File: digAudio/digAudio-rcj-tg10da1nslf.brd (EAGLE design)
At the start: 18.8 x 19.7 mm, 12 parts, among them IC1 DIT4096-H

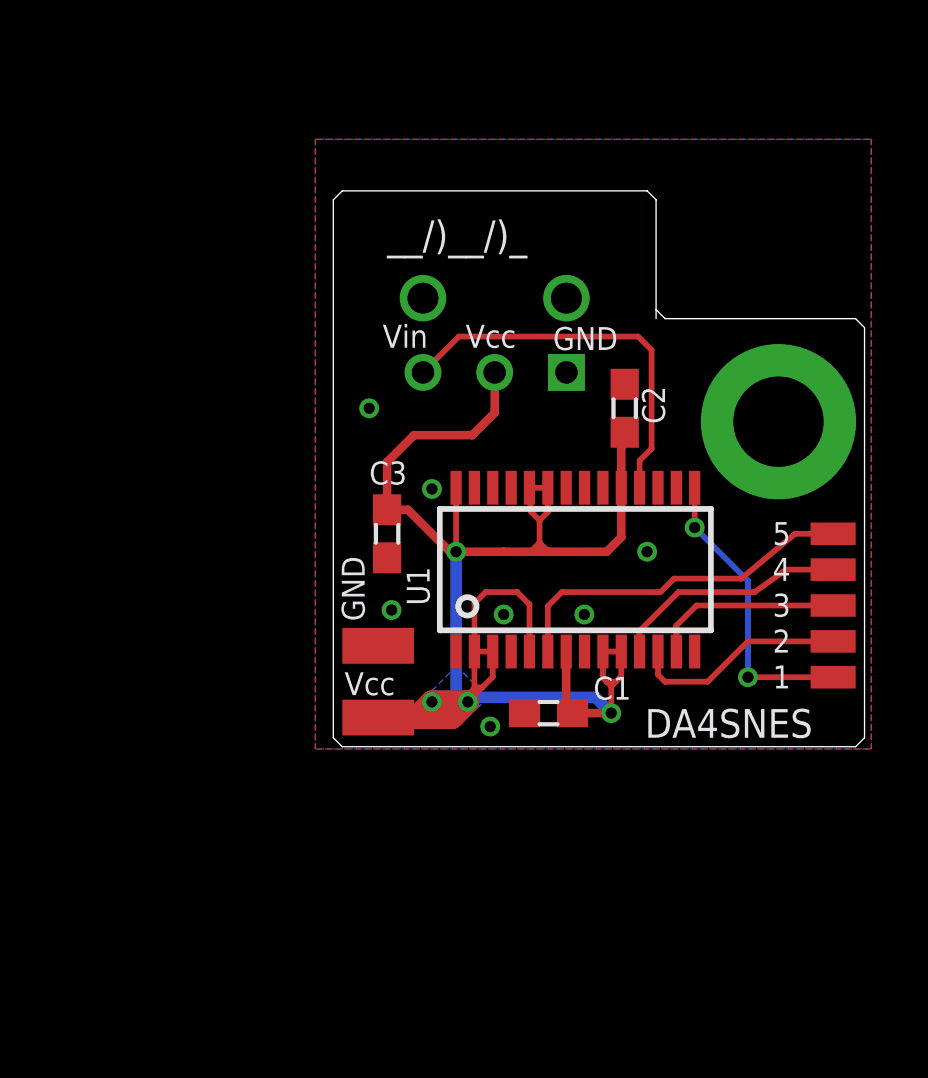
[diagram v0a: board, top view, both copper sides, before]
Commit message: update digital audio mod incl a new no-cut design with coax
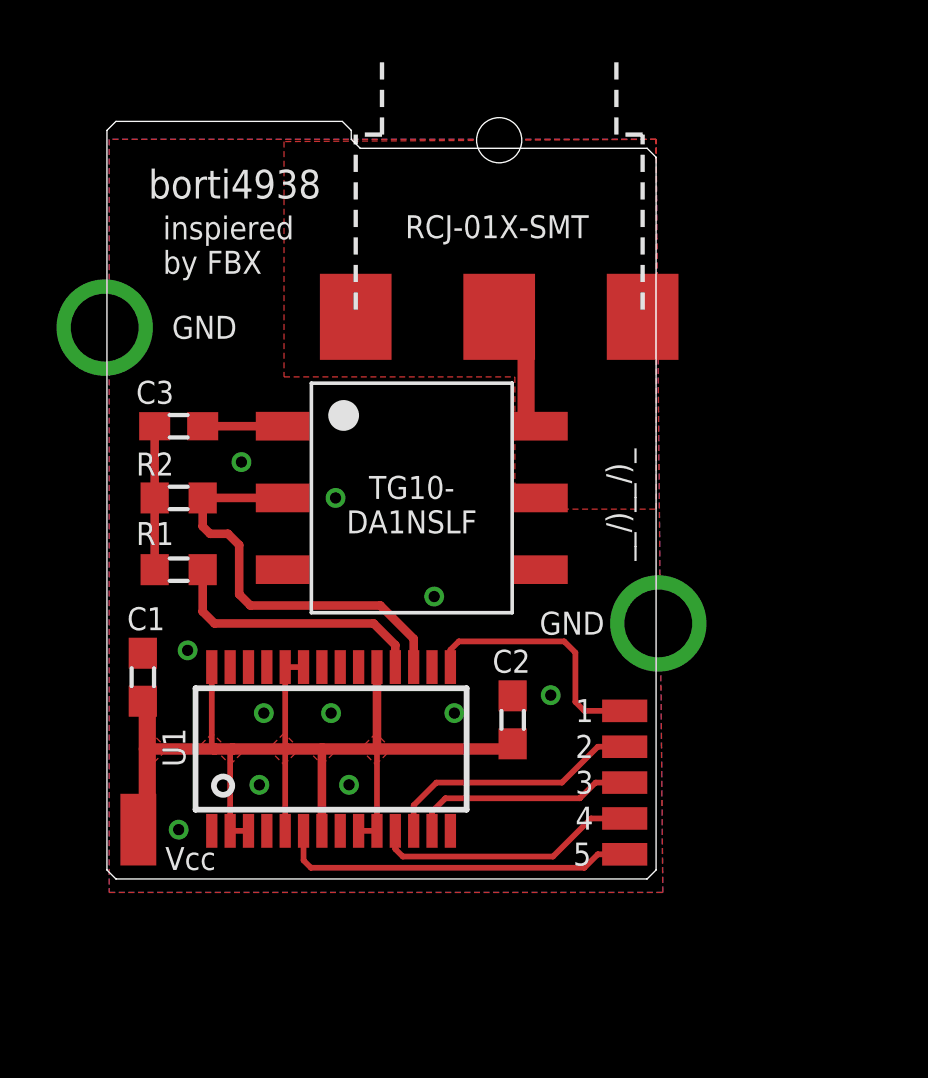
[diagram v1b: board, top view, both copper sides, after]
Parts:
- removed GND: (no value), wirepad:SMD1,27-2,54
- added R1: 360, rcl:R0603
- added R2: 91, rcl:R0603
- added U$2: TG10-DA1NSLF, cs8406:TG10-DA1NSFL
- C3: value 0.1uF -> 10nF
- U$1: value PLT133/T10W -> RCJ-013-SMT-TR; device cs8406:PLT133/T10W -> digAudio_SNES:RCJ_01X_SMT_MODIFIED
- moved C1 14.4 mm to (-6.11, 2.54), turned to 90 degrees
- moved 5 13.5 mm to (11.0, -3.73)
- moved C2 11.7 mm to (6.99, 1.03)
- moved 4 11.5 mm to (11.0, -2.46)
- moved IC1 10.7 mm to (0.56, 0.00)
- moved 3 9.69 mm to (11.0, -1.19)
- moved VCC 9.37 mm to (-6.27, -2.86), turned to 180 degrees
- moved C3 8.31 mm to (-4.84, 11.4), turned to 0 degrees
- moved 2 8.27 mm to (11.0, 0.08)
- moved 1 7.48 mm to (11.0, 1.35)
- moved U$1 2.23 mm to (6.51, 15.6), flipped to the top, turned to 270 degrees
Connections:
- new net N$10: U$1.1A, U$1.1B, U$2.5
- new net N$11: C3.2, U$2.1
- new net N$7: IC1.17, R2.1, U$2.2
- new net N$8: C3.1, R1.2, R2.2
- new net N$9: U$1.2, U$2.6
- net GND: now also U$2.3; no longer C3.2, GND.1, U$1.P$1
- net N$1: now also R1.1; no longer U$1.P$3
- net VCC: no longer C3.1, U$1.P$2
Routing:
- net VCC: track 66.8 -> 40.3 mm, vias 4 -> 0
- net N$7: track 0.00 -> 15.0 mm
- net N$9: track 0.00 -> 5.35 mm
- net N$8: track 0.00 -> 5.08 mm
- net N$1: track 13.9 -> 9.58 mm
- net N$11: track 0.00 -> 2.83 mm
- net N$2: track 10.5 -> 8.95 mm, vias 2 -> 0
- net N$3: track 7.72 -> 9.24 mm
- net N$5: track 6.77 -> 7.93 mm
- net N$4: track 8.41 -> 9.44 mm
- added copper zone on layer 1, net N$10
- added copper zone on layer 1, net VCC
- removed copper zone on layer 16, net VCC
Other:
- board size 18.8 x 19.7 mm -> 19.4 x 26.8 mm
- board text added: "Digital Audio for SNES RCA-output version"
- board text added: "R1"
- board text added: "R2"
- board text added: "RCJ-01X-SMT"
- board text added: "TG10- DA1NSLF"
- board text added: "borti4938"
- board text added: "inspiered by FBX"
- board text removed: "DA4SNES"
- board text removed: "Vin"

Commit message: PCB Update
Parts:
- added GND: (no value), wirepad:1,6/0,9
- added J1: (no value), jumper:SJ_2
- C3: value 10nF -> 10nF/0.1uF
- R1: value 360 -> 347.5/57
- R2: value 91 -> 90.9/open
- VCC: device wirepad:SMD1,27-2,54 -> wirepad:1,6/0,9
- moved VCC 12.7 mm to (5.00, -8.81), turned to 0 degrees
- moved C3 2.29 mm to (-3.57, 13.3)
- moved R2 1.02 mm to (-5.48, 9.68), turned to 270 degrees
- moved R1 0.75 mm to (-5.48, 6.75), turned to 90 degrees
- moved U$2 0.63 mm to (4.05, 8.89)
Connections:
- new net N$12: J1.2, R2.1, U$2.2
- net GND: now also GND.1, J1.1
- net N$7: now also J1.3; no longer R2.1, U$2.2
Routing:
- net VCC: track 40.3 -> 57.4 mm
- net N$12: track 0.00 -> 6.10 mm
- net N$7: track 15.0 -> 10.0 mm
- net N$8: track 5.08 -> 7.89 mm
- net N$11: track 2.83 -> 3.44 mm
- net GND: track 0.00 -> 0.56 mm, vias 13 -> 14
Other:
- board size 19.4 x 26.8 mm -> 19.4 x 31 mm
- board text added: "DA4SNES"
- board text added: "J1"
- board text added: "Tx+"
- board text added: "Tx-"
- board text added: "inspired by FBX"
- board text removed: "inspiered by FBX"
